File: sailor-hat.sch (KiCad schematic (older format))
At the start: 26 parts, among them J1 Screw_Terminal_01x04, J2 Raspberry_Pi_2_3, J3 Conn_02x07_Counter_Clockwise, J4 Screw_Terminal_01x02, J5 Screw_Terminal_01x03

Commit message: Implement better current limiting
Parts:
- removed D1: SMF16CA, Diode_SMD:D_SOD-123F, symbol Device:D_TVS
- removed D2: DS34W, Diode_SMD:D_SOD-123F, symbol Diode:1N5820
- added D?: TPSMA6L16A, Diode_SMD:D_SMA_Handsoldering, symbol Device:D_Zener
- F1: value 1A -> 2920L110/60MR (1.1A)
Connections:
- net Buck converter/Vin is gone; now on net 12V_fused: R1.1, TP1.1
- net Vcap is gone; now on net 2.65V: J4.2 (Pin_2), R20.1, TP3.1
- net 12V_fused: now also D?.1 (K)
- net GND: now also D?.2 (A)
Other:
- note added: "VcapS is scaled from 2.7V to 1.1V\n(this will also drain the caps over time)"
- note removed: "VcapS is scaled from 2.7V to 1.1V"
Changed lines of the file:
@@
 $Descr A4 11693 8268
 encoding utf-8
-Sheet 1 7
+Sheet 1 6
 Title ""
 Date ""
@@
 	9550 5100 9300 5100
 Wire Wire Line
-	2650 1300 2800 1300
+	2650 1300 2900 1300
 Connection ~ 2650 1300
 $Sheet
@@
 AR Path="/5C3476D8/5CA75C67" Ref="F?"  Part="1"
 F 0 "F1" V 903 1300 50  0000 C CNN
-F 1 "1A" V 994 1300 50  0000 C CNN
+F 1 "2920L110/60MR (1.1A)" V 994 1300 50  0000 C CNN
 F 2 "Fuse:Fuse_1206_3216Metric_Pad1.42x1.75mm_HandSolder" V 1030 1300 50  0001 C CNN
 F 3 "~" H 1100 1300 50  0001 C CNN
@@
 	1    0    0    -1
 $EndComp
-$Comp
-L Diode:1N5820 D?
-U 1 1 5CA75C84
-P 1850 1300
-AR Path="/5C3480BB/5CA75C84" Ref="D?"  Part="1"
-AR Path="/5C3476D8/5CA75C84" Ref="D?"  Part="1"
-AR Path="/5C345D5A/5CA75C84" Ref="D?"  Part="1"
-AR Path="/5CA75C84" Ref="D2"  Part="1"
-F 0 "D2" H 1700 1200 50  0000 L CNN
-F 1 "DS34W" V 1900 950 50  0000 L CNN
-F 2 "Diode_SMD:D_SOD-123F" H 1850 1125 50  0001 C CNN
-F 3 "http://www.vishay.com/docs/88526/1n5820.pdf" H 1850 1300 50  0001 C CNN
-	1    1850 1300
-	-1   0    0    1
-$EndComp
-Wire Wire Line
-	2000 1300 2200 1300
 Wire Wire Line
 	950  1300 850  1300
-Text Label 1600 1300 1    50   ~ 0
+Text Label 1800 1300 1    50   ~ 0
 12V_fused
-$Comp
-L Device:D_TVS D?
-U 1 1 5CA75C8F
-P 1550 1600
-AR Path="/5C3476D8/5CA75C8F" Ref="D?"  Part="1"
-AR Path="/5CA75C8F" Ref="D1"  Part="1"
-F 0 "D1" V 1504 1679 50  0000 L CNN
-F 1 "SMF16CA" V 1595 1679 50  0000 L CNN
-F 2 "Diode_SMD:D_SOD-123F" H 1550 1600 50  0001 C CNN
-F 3 "~" H 1550 1600 50  0001 C CNN
-	1    1550 1600
-	0    1    1    0
-$EndComp
 $Comp
 L power:GND #PWR02
 U 1 1 5CA75C96
-P 1550 1900
+P 1400 1900
 AR Path="/5CA75C96" Ref="#PWR02"  Part="1"
 AR Path="/5C3476D8/5CA75C96" Ref="#PWR?"  Part="1"
-F 0 "#PWR02" H 1550 1650 50  0001 C CNN
-F 1 "GND" H 1555 1727 50  0000 C CNN
-F 2 "" H 1550 1900 50  0001 C CNN
-F 3 "" H 1550 1900 50  0001 C CNN
-	1    1550 1900
-	1    0    0    -1
-$EndComp
-Wire Wire Line
-	1550 1900 1550 1750
-Wire Wire Line
-	1550 1450 1550 1300
-Connection ~ 1550 1300
-Wire Wire Line
-	1550 1300 1700 1300
+F 0 "#PWR02" H 1400 1650 50  0001 C CNN
+F 1 "GND" H 1405 1727 50  0000 C CNN
+F 2 "" H 1400 1900 50  0001 C CNN
+F 3 "" H 1400 1900 50  0001 C CNN
+	1    1400 1900
+	1    0    0    -1
+$EndComp
+Wire Wire Line
+	1400 1900 1400 1750
+Wire Wire Line
+	1400 1450 1400 1300
 Connection ~ 2200 1300
 Wire Wire Line
@@
 L power:PWR_FLAG #FLG0102
 U 1 1 5CA83444
-P 1450 1300
-F 0 "#FLG0102" H 1450 1375 50  0001 C CNN
-F 1 "PWR_FLAG" H 1450 1474 50  0000 C CNN
-F 2 "" H 1450 1300 50  0001 C CNN
-F 3 "~" H 1450 1300 50  0001 C CNN
-	1    1450 1300
-	1    0    0    -1
-$EndComp
-Connection ~ 1450 1300
-Wire Wire Line
-	1450 1300 1550 1300
+P 1650 1300
+F 0 "#FLG0102" H 1650 1375 50  0001 C CNN
+F 1 "PWR_FLAG" H 1650 1474 50  0000 C CNN
+F 2 "" H 1650 1300 50  0001 C CNN
+F 3 "~" H 1650 1300 50  0001 C CNN
+	1    1650 1300
+	1    0    0    -1
+$EndComp
+Connection ~ 1650 1300
 Wire Wire Line
 	2200 1300 2650 1300
-Wire Wire Line
-	1250 1300 1450 1300
 $Comp
 L Device:R R20
@@
 Connection ~ 6550 1300
 $Sheet
-S 3800 1150 700  500
-U 5CA852AD
-F0 "Current limiting" 50
-F1 "current_limiting.sch" 50
-F2 "Vin" I L 3800 1300 50
-F3 "Vilim" O R 4500 1300 50
-F4 "ENIN" I L 3800 1500 50
-$EndSheet
-Wire Wire Line
-	4500 1300 4750 1300
-Wire Wire Line
-	3800 1300 3600 1300
-$Sheet
-S 2800 1150 650  500
+S 2900 1150 650  500
 U 5CA65CC5
 F0 "Buck converter" 50
 F1 "buck.sch" 50
-F2 "Vin" I L 2800 1300 50
-F3 "Vbuck" O R 3450 1300 50
+F2 "Vin" I L 2900 1300 50
+F3 "Vbuck" O R 3550 1300 50
+F4 "ENIN" I L 2900 1500 50
 $EndSheet
-Wire Wire Line
-	3600 1300 3450 1300
-Connection ~ 3600 1300
 Connection ~ 4750 1300
 Wire Wire Line
@@
 NoConn ~ 8900 2250
 NoConn ~ 8900 3450
-Text GLabel 3600 800  1    50   Input ~ 0
+Text GLabel 4200 800  1    50   Input ~ 0
 2.65V
 Wire Wire Line
-	3600 800  3600 900
+	4200 800  4200 900
 Text Label 2950 2950 2    50   ~ 0
 ATT_Vcc
@@
 	1    0    0    -1
 $EndComp
-Text Notes 5100 5300 0    50   ~ 0
-VcapS is scaled from 2.7V to 1.1V
-Connection ~ 3600 900
-Wire Wire Line
-	3600 900  3600 1300
+Text Notes 4900 5300 0    50   ~ 0
+VcapS is scaled from 2.7V to 1.1V\n(this will also drain the caps over time)
+Connection ~ 4200 900
+Wire Wire Line
+	4200 900  4200 1300
 $Comp
 L power:PWR_FLAG #FLG0101
 U 1 1 5CF2FDF8
-P 3600 900
-F 0 "#FLG0101" H 3600 975 50  0001 C CNN
-F 1 "PWR_FLAG" V 3600 1200 50  0000 C CNN
-F 2 "" H 3600 900 50  0001 C CNN
-F 3 "~" H 3600 900 50  0001 C CNN
-	1    3600 900
-	0    -1   -1   0
-$EndComp
-Wire Wire Line
-	3650 1500 3650 1950
-Wire Wire Line
-	3650 1500 3800 1500
-Text Label 3650 1950 0    50   ~ 0
+P 4200 900
+F 0 "#FLG0101" H 4200 975 50  0001 C CNN
+F 1 "PWR_FLAG" V 4200 1200 50  0000 C CNN
+F 2 "" H 4200 900 50  0001 C CNN
+F 3 "~" H 4200 900 50  0001 C CNN
+	1    4200 900
+	0    -1   -1   0
+$EndComp
+Wire Wire Line
+	2800 1500 2800 1950
+Text Label 2800 1950 0    50   ~ 0
 ENIN
+$Comp
+L Device:D_Zener D?
+U 1 1 5E20D410
+P 1400 1600
+F 0 "D?" V 1354 1521 50  0000 R CNN
+F 1 "TPSMA6L16A" V 1445 1521 50  0000 R CNN
+F 2 "Diode_SMD:D_SMA_Handsoldering" H 1400 1600 50  0001 C CNN
+F 3 "~" H 1400 1600 50  0001 C CNN
+	1    1400 1600
+	0    -1   1    0
+$EndComp
+Wire Wire Line
+	1250 1300 1400 1300
+Connection ~ 1400 1300
+Wire Wire Line
+	1400 1300 1650 1300
+Wire Wire Line
+	1650 1300 2200 1300
+Wire Wire Line
+	2900 1500 2800 1500
+Connection ~ 4200 1300
+Wire Wire Line
+	4200 1300 4750 1300
+Wire Wire Line
+	3550 1300 4200 1300
 $EndSCHEMATC

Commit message: Annotate and tweak power flags
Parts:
- gave numbers to parts that had none: 1
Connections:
- net 2.65V renamed Vcap
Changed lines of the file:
@@
 Wire Wire Line
 	9750 5100 9550 5100
-$Comp
-L power:PWR_FLAG #FLG03
-U 1 1 5C391989
-P 9300 5100
-F 0 "#FLG03" H 9300 5175 50  0001 C CNN
-F 1 "PWR_FLAG" H 9300 5274 50  0000 C CNN
-F 2 "" H 9300 5100 50  0001 C CNN
-F 3 "~" H 9300 5100 50  0001 C CNN
-	1    9300 5100
-	-1   0    0    1
-$EndComp
-Wire Wire Line
-	9900 1100 9900 1250
-$Comp
-L power:PWR_FLAG #FLG04
-U 1 1 5C393112
-P 9900 1250
-F 0 "#FLG04" H 9900 1325 50  0001 C CNN
-F 1 "PWR_FLAG" V 9900 1378 50  0000 L CNN
-F 2 "" H 9900 1250 50  0001 C CNN
-F 3 "~" H 9900 1250 50  0001 C CNN
-	1    9900 1250
-	0    1    1    0
-$EndComp
-Connection ~ 9900 1250
 Text Label 4300 2800 0    50   ~ 0
 ATT_RESET
@@
 $EndComp
 Connection ~ 9550 5100
-Wire Wire Line
-	9550 5100 9300 5100
 Wire Wire Line
 	2650 1300 2900 1300
@@
 L power:GND #PWR02
 U 1 1 5CA75C96
-P 1400 1900
+P 1400 2400
 AR Path="/5CA75C96" Ref="#PWR02"  Part="1"
 AR Path="/5C3476D8/5CA75C96" Ref="#PWR?"  Part="1"
-F 0 "#PWR02" H 1400 1650 50  0001 C CNN
-F 1 "GND" H 1405 1727 50  0000 C CNN
-F 2 "" H 1400 1900 50  0001 C CNN
-F 3 "" H 1400 1900 50  0001 C CNN
-	1    1400 1900
-	1    0    0    -1
-$EndComp
-Wire Wire Line
-	1400 1900 1400 1750
+F 0 "#PWR02" H 1400 2150 50  0001 C CNN
+F 1 "GND" H 1405 2227 50  0000 C CNN
+F 2 "" H 1400 2400 50  0001 C CNN
+F 3 "" H 1400 2400 50  0001 C CNN
+	1    1400 2400
+	1    0    0    -1
+$EndComp
 Wire Wire Line
 	1400 1450 1400 1300
@@
 Wire Wire Line
 	4750 1300 5050 1300
-$Comp
-L power:PWR_FLAG #FLG0102
-U 1 1 5CA83444
-P 1650 1300
-F 0 "#FLG0102" H 1650 1375 50  0001 C CNN
-F 1 "PWR_FLAG" H 1650 1474 50  0000 C CNN
-F 2 "" H 1650 1300 50  0001 C CNN
-F 3 "~" H 1650 1300 50  0001 C CNN
-	1    1650 1300
-	1    0    0    -1
-$EndComp
-Connection ~ 1650 1300
 Wire Wire Line
 	2200 1300 2650 1300
@@
 	0    -1   -1   0
 $EndComp
-$Comp
-L power:PWR_FLAG #FLG01
-U 1 1 5C3903CF
-P 6150 1300
-F 0 "#FLG01" H 6150 1375 50  0001 C CNN
-F 1 "PWR_FLAG" H 6150 1474 50  0000 C CNN
-F 2 "" H 6150 1300 50  0001 C CNN
-F 3 "~" H 6150 1300 50  0001 C CNN
-	1    6150 1300
-	1    0    0    -1
-$EndComp
 Wire Wire Line
 	6550 1300 6800 1300
@@
 NoConn ~ 8900 2250
 NoConn ~ 8900 3450
-Text GLabel 4200 800  1    50   Input ~ 0
-2.65V
-Wire Wire Line
-	4200 800  4200 900
 Text Label 2950 2950 2    50   ~ 0
 ATT_Vcc
@@
 Wire Wire Line
 	9500 1450 9500 1550
-Wire Wire Line
-	9800 1550 9800 1400
 Wire Wire Line
 	4150 4550 4300 4550
@@
 Text Label 4300 5750 0    50   ~ 0
 GPIO2
-Wire Wire Line
-	9300 5100 9150 5100
-Connection ~ 9300 5100
 Text Notes 5100 4050 0    50   ~ 0
 0R resistors allow for disabling or re-routing\nsignals connected to Raspi GPIOs
-Wire Wire Line
-	9900 1250 9900 1550
-Text GLabel 9800 1400 1    50   Input ~ 0
+Text GLabel 9800 1100 1    50   Input ~ 0
 3.3V
 $Comp
@@
 Text Notes 4900 5300 0    50   ~ 0
 VcapS is scaled from 2.7V to 1.1V\n(this will also drain the caps over time)
-Connection ~ 4200 900
-Wire Wire Line
-	4200 900  4200 1300
-$Comp
-L power:PWR_FLAG #FLG0101
-U 1 1 5CF2FDF8
-P 4200 900
-F 0 "#FLG0101" H 4200 975 50  0001 C CNN
-F 1 "PWR_FLAG" V 4200 1200 50  0000 C CNN
-F 2 "" H 4200 900 50  0001 C CNN
-F 3 "~" H 4200 900 50  0001 C CNN
-	1    4200 900
-	0    -1   -1   0
-$EndComp
 Wire Wire Line
 	2800 1500 2800 1950
@@
 ENIN
 $Comp
-L Device:D_Zener D?
+L Device:D_Zener D1
 U 1 1 5E20D410
 P 1400 1600
-F 0 "D?" V 1354 1521 50  0000 R CNN
+F 0 "D1" V 1354 1521 50  0000 R CNN
 F 1 "TPSMA6L16A" V 1445 1521 50  0000 R CNN
 F 2 "Diode_SMD:D_SMA_Handsoldering" H 1400 1600 50  0001 C CNN
@@
 Connection ~ 1400 1300
 Wire Wire Line
-	1400 1300 1650 1300
-Wire Wire Line
-	1650 1300 2200 1300
-Wire Wire Line
 	2900 1500 2800 1500
-Connection ~ 4200 1300
-Wire Wire Line
-	4200 1300 4750 1300
-Wire Wire Line
-	3550 1300 4200 1300
 $Comp
 L Connector:TestPoint TP?
@@
 	1    0    0    -1
 $EndComp
+Wire Wire Line
+	3550 1300 4750 1300
+Wire Wire Line
+	1400 1300 2200 1300
+Wire Wire Line
+	9150 5100 9550 5100
+Wire Wire Line
+	9900 1100 9900 1550
+Wire Wire Line
+	9800 1100 9800 1550
+Wire Wire Line
+	1400 1750 1400 2250
+$Comp
+L power:PWR_FLAG #FLG0102
+U 1 1 5E2C97C1
+P 1400 2250
+F 0 "#FLG0102" H 1400 2325 50  0001 C CNN
+F 1 "PWR_FLAG" V 1400 2378 50  0000 L CNN
+F 2 "" H 1400 2250 50  0001 C CNN
+F 3 "~" H 1400 2250 50  0001 C CNN
+	1    1400 2250
+	0    1    1    0
+$EndComp
+Connection ~ 1400 2250
+Wire Wire Line
+	1400 2250 1400 2400
 $EndSCHEMATC

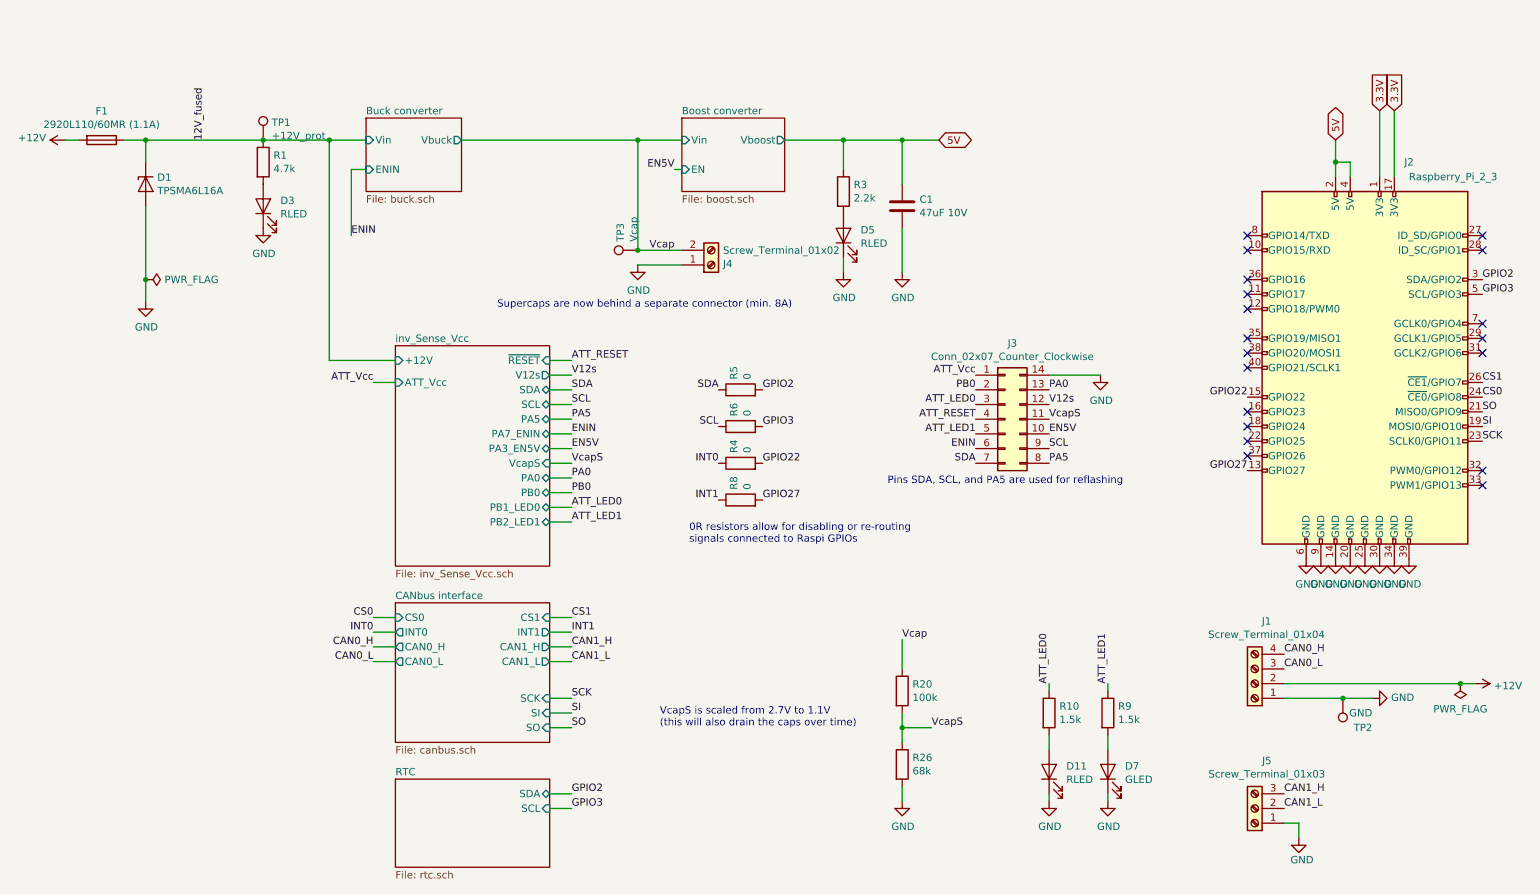
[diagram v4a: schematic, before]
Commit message: Update licence, tweaks to footprints and ERC
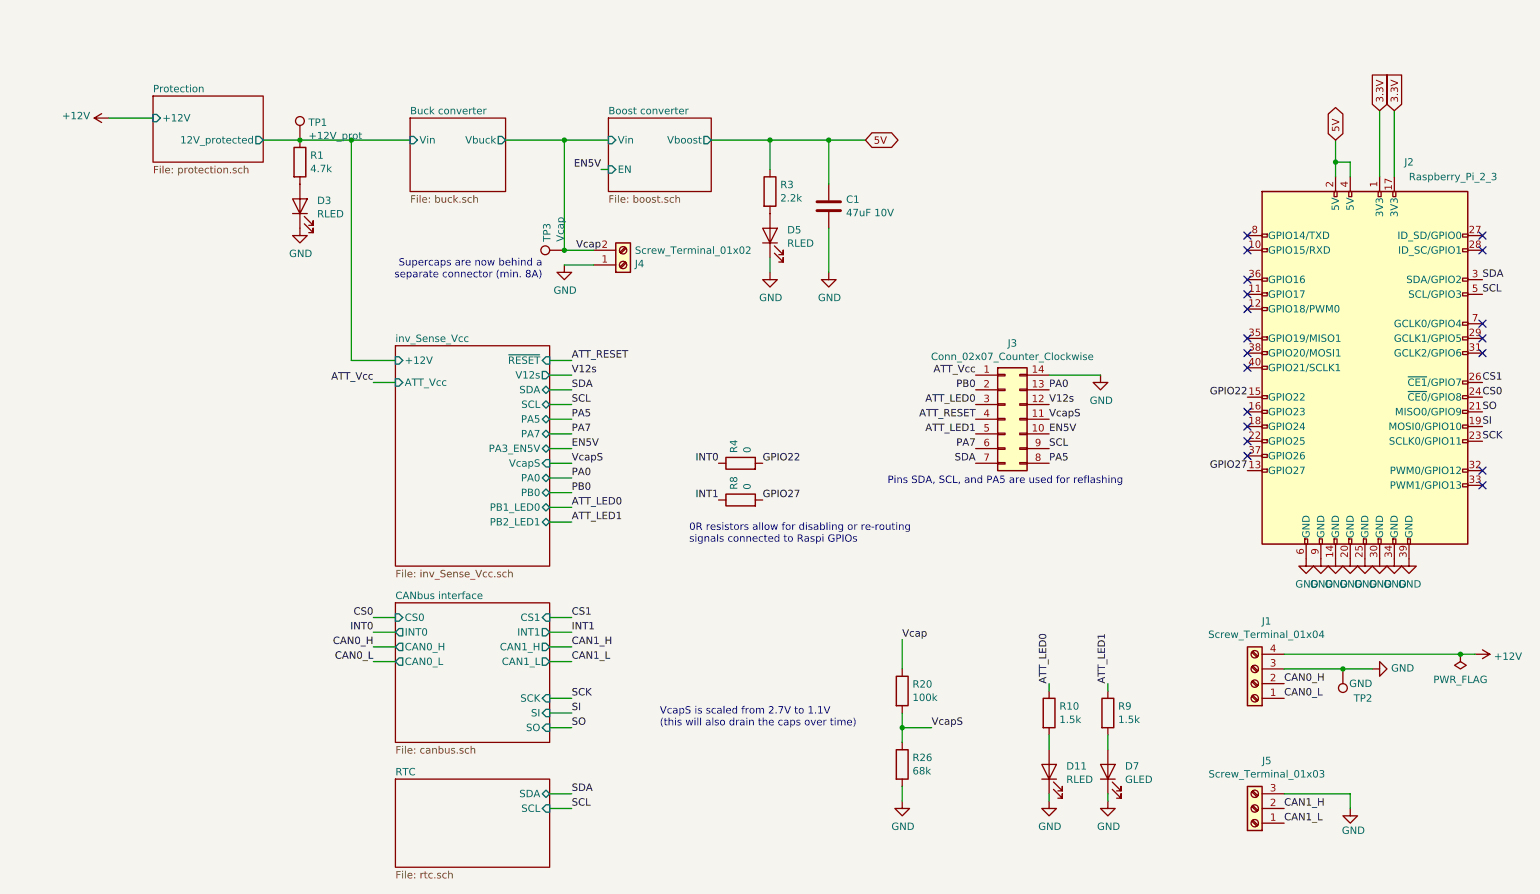
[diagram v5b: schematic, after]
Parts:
- removed D1: TPSMA6L16A, Diode_SMD:D_SMA_Handsoldering, symbol Device:D_Zener
- removed F1: 2920L110/60MR (1.1A), Fuse:Fuse_1206_3216Metric_Pad1.42x1.75mm_HandSolder, symbol Device:Fuse
- removed R5, R6: 0, Resistor_SMD:R_0603_1608Metric_Pad1.05x0.95mm_HandSolder, symbol Device:R
- C1: footprint Capacitor_SMD:C_0805_2012Metric_Pad1.15x1.40mm_HandSolder -> Capacitor_SMD:C_1210_3225Metric
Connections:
- net GPIO2 is gone; now on net SDA: J2.3 (SDA/GPIO2)
- net GPIO3 is gone; now on net SCL: J2.5 (SCL/GPIO3)
- net +12V: now also J1.4 (Pin_4); no longer J1.2 (Pin_2)
- net CAN0_H: now also J1.2 (Pin_2); no longer J1.4 (Pin_4)
- net CAN0_L: now also J1.1 (Pin_1); no longer J1.3 (Pin_3)
- net CAN1_H: now also J5.2 (Pin_2); no longer J5.3 (Pin_3)
- net CAN1_L: now also J5.1 (Pin_1); no longer J5.2 (Pin_2)
- net GND: now also J1.3 (Pin_3), J5.3 (Pin_3); no longer J1.1 (Pin_1), J5.1 (Pin_1)
- net Vcap: no longer J4.2 (Pin_2), TP3.1
- net 12V_fused renamed Buck converter/Vin
- net ENIN renamed PA7
- new net Boost converter/Vin: J4.2 (Pin_2), TP3.1
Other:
- note added: "Supercaps are now behind a\nseparate connector (min. 8A)"
- note removed: "Supercaps are now behind a separate connector (min. 8A)"
- moved on the sheet: C1, D3, D5, J4, R1, R3, TP1, TP2, TP3

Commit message: Update the README, add a new rendered image of the board
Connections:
- net Boost converter/Vin is gone; now on net Vcap: J4.2 (Pin_2), TP3.1
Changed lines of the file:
@@
 Wire Wire Line
 	4250 1300 4250 2050
-Text Label 4500 2050 2    50   ~ 0
+Text Label 4250 1700 2    50   ~ 0
 Vcap
 Text Label 10500 2250 0    50   ~ 0
@@
 F0 "inv_Sense_Vcc" 50
 F1 "inv_Sense_Vcc.sch" 50
-F2 "+12V" I L 3100 2800 50
+F2 "12V_prot" I L 3100 2800 50
 F3 "~RESET~" I R 4150 2800 50
 F4 "V12s" O R 4150 2900 50

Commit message: Swap CAN0 and CAN1 connectors; use GPIO 5 & 6 for CAN interrupts for Moitessier compatibility
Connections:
- net CAN0_H: now also J5.2 (Pin_2); no longer J1.2 (Pin_2)
- net CAN0_L: now also J5.1 (Pin_1); no longer J1.1 (Pin_1)
- net CAN1_H: now also J1.2 (Pin_2); no longer J5.2 (Pin_2)
- net CAN1_L: now also J1.1 (Pin_1); no longer J5.1 (Pin_1)
- net GPIO5: now reaches J2.29 (GCLK1/GPIO5)
- net GPIO5: now also R4.2
- net GPIO6: now reaches J2.31 (GCLK2/GPIO6)
- net GPIO6: now also R8.2
- net GPIO22: no longer names the net of J2.15 (GPIO22)
- net GPIO22: no longer R4.2
- net GPIO27: no longer names the net of J2.13 (GPIO27)
- net GPIO27: no longer R8.2
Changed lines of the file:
@@
 NoConn ~ 8900 3250
 NoConn ~ 10500 3550
-NoConn ~ 10500 2750
-NoConn ~ 10500 2650
 NoConn ~ 10500 2550
 NoConn ~ 10500 2050
@@
 INT0
 Text Label 5600 3500 0    50   ~ 0
-GPIO22
+GPIO5
 Text Label 5300 3750 2    50   ~ 0
 INT1
 Text Label 5600 3750 0    50   ~ 0
-GPIO27
+GPIO6
 $Comp
 L Device:R R8
@@
 $EndComp
 Text Label 9150 5000 0    50   ~ 0
-CAN0_H
+CAN1_H
 Text Label 9150 5100 0    50   ~ 0
-CAN0_L
+CAN1_L
 $Comp
 L Connector:Screw_Terminal_01x03 J5
@@
 $EndComp
 Text Label 9150 5850 0    50   ~ 0
-CAN1_H
+CAN0_H
 Text Label 9150 5950 0    50   ~ 0
-CAN1_L
+CAN0_L
 $Comp
 L Connector:Screw_Terminal_01x02 J4
@@
 Wire Wire Line
 	9150 5750 9600 5750
-Text Label 8900 3550 2    50   ~ 0
-GPIO27
-Text Label 8900 3050 2    50   ~ 0
-GPIO22
 Connection ~ 2800 1300
 $Comp
@@
 	4250 1300 3850 1300
 Connection ~ 4250 1300
+NoConn ~ 8900 3050
+NoConn ~ 8900 3550
+Text Label 10500 2650 0    50   ~ 0
+GPIO5
+Text Label 10500 2750 0    50   ~ 0
+GPIO6
 $EndSCHEMATC

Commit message: Add LCSC part numbers to components
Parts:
- C1: LCSC (none) -> C77101
- D11, D3, D5: LCSC (none) -> C2286
- D7: LCSC (none) -> C72043
- R1: LCSC (none) -> C23162
- R10, R9: LCSC (none) -> C22843
- R20: LCSC (none) -> C25803
- R26: LCSC (none) -> C23231
- R3: LCSC (none) -> C4190
- R4, R8: LCSC (none) -> C21189
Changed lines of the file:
@@
 F 2 "Resistor_SMD:R_0603_1608Metric_Pad1.05x0.95mm_HandSolder" V 6480 5050 50  0001 C CNN
 F 3 "~" H 6550 5050 50  0001 C CNN
+F 4 "C25803" H 6550 5050 50  0001 C CNN "LCSC"
 	1    6550 5050
 	1    0    0    -1
@@
 F 2 "LED_SMD:LED_0603_1608Metric_Pad1.05x0.95mm_HandSolder" H 7550 5600 50  0001 C CNN
 F 3 "~" H 7550 5600 50  0001 C CNN
+F 4 "C2286" H 7550 5600 50  0001 C CNN "LCSC"
 	1    7550 5600
 	0    -1   -1   0
@@
 F 2 "Resistor_SMD:R_0603_1608Metric_Pad1.05x0.95mm_HandSolder" V 7480 5200 50  0001 C CNN
 F 3 "~" H 7550 5200 50  0001 C CNN
+F 4 "C22843" H 7550 5200 50  0001 C CNN "LCSC"
 	1    7550 5200
 	1    0    0    -1
@@
 F 2 "LED_SMD:LED_0603_1608Metric_Pad1.05x0.95mm_HandSolder" H 7950 5600 50  0001 C CNN
 F 3 "~" H 7950 5600 50  0001 C CNN
+F 4 "C72043" H 7950 5600 50  0001 C CNN "LCSC"
 	1    7950 5600
 	0    -1   -1   0
@@
 F 2 "Resistor_SMD:R_0603_1608Metric_Pad1.05x0.95mm_HandSolder" V 7880 5200 50  0001 C CNN
 F 3 "~" H 7950 5200 50  0001 C CNN
+F 4 "C22843" H 7950 5200 50  0001 C CNN "LCSC"
 	1    7950 5200
 	1    0    0    -1
@@
 F 2 "Capacitor_SMD:C_1210_3225Metric" H 6088 1600 50  0001 C CNN
 F 3 "~" H 6050 1750 50  0001 C CNN
+F 4 "C77101" H 6050 1750 50  0001 C CNN "LCSC"
 	1    6050 1750
 	1    0    0    -1
@@
 F 2 "Resistor_SMD:R_0603_1608Metric_Pad1.05x0.95mm_HandSolder" V 5580 1650 50  0001 C CNN
 F 3 "~" H 5650 1650 50  0001 C CNN
+F 4 "C4190" H 5650 1650 50  0001 C CNN "LCSC"
 	1    5650 1650
 	1    0    0    -1
@@
 F 2 "LED_SMD:LED_0603_1608Metric_Pad1.05x0.95mm_HandSolder" H 5650 1950 50  0001 C CNN
 F 3 "~" H 5650 1950 50  0001 C CNN
+F 4 "C2286" H 5650 1950 50  0001 C CNN "LCSC"
 	1    5650 1950
 	0    -1   -1   0
@@
 F 2 "Resistor_SMD:R_0603_1608Metric_Pad1.05x0.95mm_HandSolder" V 5380 3500 50  0001 C CNN
 F 3 "~" H 5450 3500 50  0001 C CNN
+F 4 "C21189" H 5450 3500 50  0001 C CNN "LCSC"
 	1    5450 3500
 	0    -1   -1   0
@@
 F 2 "Resistor_SMD:R_0603_1608Metric_Pad1.05x0.95mm_HandSolder" V 5380 3750 50  0001 C CNN
 F 3 "~" H 5450 3750 50  0001 C CNN
+F 4 "C21189" H 5450 3750 50  0001 C CNN "LCSC"
 	1    5450 3750
 	0    -1   -1   0
@@
 F 2 "Resistor_SMD:R_0603_1608Metric_Pad1.05x0.95mm_HandSolder" V 6480 5550 50  0001 C CNN
 F 3 "~" H 6550 5550 50  0001 C CNN
+F 4 "C23231" H 6550 5550 50  0001 C CNN "LCSC"
 	1    6550 5550
 	1    0    0    -1
@@
 F 2 "Resistor_SMD:R_0603_1608Metric_Pad1.05x0.95mm_HandSolder" V 2380 1450 50  0001 C CNN
 F 3 "~" H 2450 1450 50  0001 C CNN
+F 4 "C23162" H 2450 1450 50  0001 C CNN "LCSC"
 	1    2450 1450
 	1    0    0    -1
@@
 F 2 "LED_SMD:LED_0603_1608Metric_Pad1.05x0.95mm_HandSolder" H 2450 1750 50  0001 C CNN
 F 3 "~" H 2450 1750 50  0001 C CNN
+F 4 "C2286" H 2450 1750 50  0001 C CNN "LCSC"
 	1    2450 1750
 	0    -1   -1   0
